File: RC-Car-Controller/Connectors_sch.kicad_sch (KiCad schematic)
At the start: 8 parts, among them J1 Conn_01x02, J5 MCU_IF, J6 ANT_IF, J7 2171790001, U2 USBLC6-2SC6

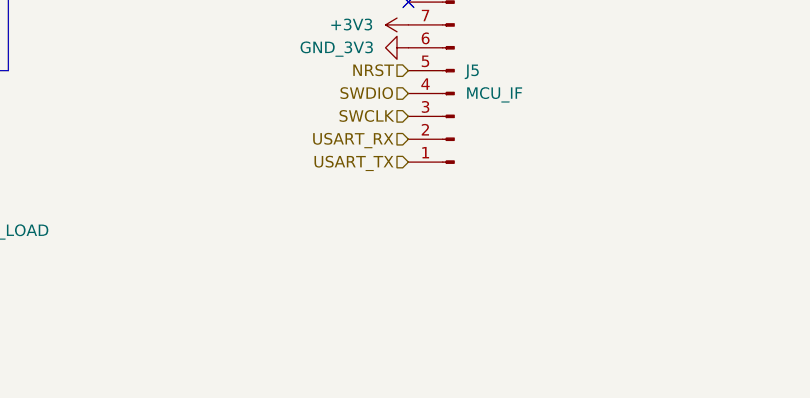
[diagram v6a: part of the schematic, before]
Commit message: Added FGH100M footprint/schematic
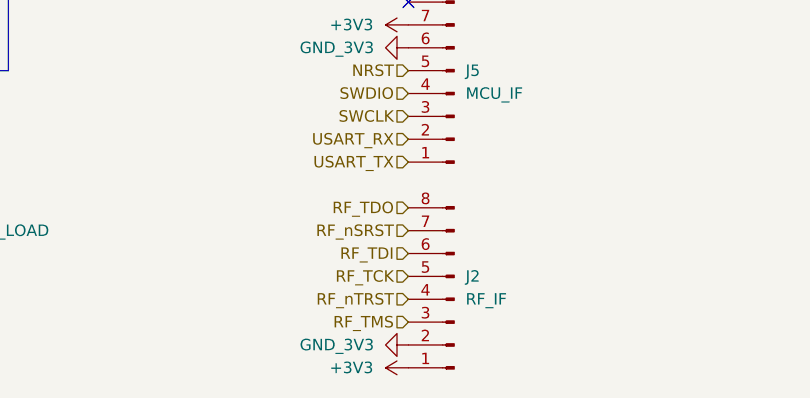
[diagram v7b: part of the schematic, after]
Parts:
- added J2: RF_IF, Connector_PinHeader_2.54mm:PinHeader_2x04_P2.54mm_Vertical, symbol Connector:Conn_01x08_Pin
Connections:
- net +3V3: now also J2.1 (Pin_1)
- net GND_3V3: now also J2.2 (Pin_2)
- new net RF_TCK: J2.5 (Pin_5)
- new net RF_TDI: J2.6 (Pin_6)
- new net RF_TDO: J2.8 (Pin_8)
- new net RF_TMS: J2.3 (Pin_3)
- new net RF_nSRST: J2.7 (Pin_7)
- new net RF_nTRST: J2.4 (Pin_4)

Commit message: Finished Controller PCB Pre-Review
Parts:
- renumbered J7 to J2, J5 to J3, J2 to J4, J6 to J5, R24 to R4, R23 to R5, U2 to U1
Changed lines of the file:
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@@
 		(on_board yes)
 		(dnp no)
-		(property "Reference" "U2"
+		(property "Reference" "U1"
 			(at 123.444 72.136 0)
 			(effects
@@
 			(project "RC-Car-Controller"
 				(path "/ba870fd1-751d-4755-8e1a-1ea86ca9e2f6/47812da9-b622-4bda-8507-4e09448e1ff5"
-					(reference "U2")
+					(reference "U1")
 					(unit 1)
 				)
@@
 		(dnp no)
 		(fields_autoplaced yes)
-		(property "Reference" "#PWR09"
+		(property "Reference" "#PWR031"
 			(at 127 129.54 0)
 			(effects
@@
 			(project "RC-Car-Project"
 				(path "/ba870fd1-751d-4755-8e1a-1ea86ca9e2f6/47812da9-b622-4bda-8507-4e09448e1ff5"
-					(reference "#PWR09")
+					(reference "#PWR031")
 					(unit 1)
 				)
@@
 		(dnp no)
 		(fields_autoplaced yes)
-		(property "Reference" "J5"
+		(property "Reference" "J3"
 			(at 129.54 134.6199 0)
 			(effects
@@
 			(project ""
 				(path "/ba870fd1-751d-4755-8e1a-1ea86ca9e2f6/47812da9-b622-4bda-8507-4e09448e1ff5"
-					(reference "J5")
+					(reference "J3")
 					(unit 1)
 				)
@@
 		(on_board yes)
 		(dnp no)
-		(property "Reference" "#PWR088"
+		(property "Reference" "#PWR028"
 			(at 104.14 110.49 0)
 			(effects
@@
 			(project "RC-Car-Controller"
 				(path "/ba870fd1-751d-4755-8e1a-1ea86ca9e2f6/47812da9-b622-4bda-8507-4e09448e1ff5"
-					(reference "#PWR088")
+					(reference "#PWR028")
 					(unit 1)
 				)
@@
 		(on_board yes)
 		(dnp no)
-		(property "Reference" "R24"
+		(property "Reference" "R4"
 			(at 104.14 90.678 90)
 			(effects
@@
 			(project "RC-Car-Controller"
 				(path "/ba870fd1-751d-4755-8e1a-1ea86ca9e2f6/47812da9-b622-4bda-8507-4e09448e1ff5"
-					(reference "R24")
+					(reference "R4")
 					(unit 1)
 				)
@@
 		(dnp no)
 		(fields_autoplaced yes)
-		(property "Reference" "J7"
+		(property "Reference" "J2"
 			(at 83.82 60.96 0)
 			(effects
@@
 			(project ""
 				(path "/ba870fd1-751d-4755-8e1a-1ea86ca9e2f6/47812da9-b622-4bda-8507-4e09448e1ff5"
-					(reference "J7")
+					(reference "J2")
 					(unit 1)
 				)
@@
 		(dnp no)
 		(fields_autoplaced yes)
-		(property "Reference" "#PWR013"
+		(property "Reference" "#PWR027"
 			(at 66.04 152.4 0)
 			(effects
@@
 			(project "RC-Car-Controller"
 				(path "/ba870fd1-751d-4755-8e1a-1ea86ca9e2f6/47812da9-b622-4bda-8507-4e09448e1ff5"
-					(reference "#PWR013")
+					(reference "#PWR027")
 					(unit 1)
 				)
@@
 		(dnp no)
 		(fields_autoplaced yes)
-		(property "Reference" "#PWR08"
+		(property "Reference" "#PWR032"
 			(at 116.84 132.08 0)
 			(effects
@@
 			(project "RC-Car-Project"
 				(path "/ba870fd1-751d-4755-8e1a-1ea86ca9e2f6/47812da9-b622-4bda-8507-4e09448e1ff5"
-					(reference "#PWR08")
+					(reference "#PWR032")
 					(unit 1)
 				)
@@
 		(dnp no)
 		(fields_autoplaced yes)
-		(property "Reference" "J2"
+		(property "Reference" "J4"
 			(at 129.54 157.4799 0)
 			(effects
@@
 			(project "RC-Car-Controller"
 				(path "/ba870fd1-751d-4755-8e1a-1ea86ca9e2f6/47812da9-b622-4bda-8507-4e09448e1ff5"
-					(reference "J2")
+					(reference "J4")
 					(unit 1)
 				)
@@
 		(dnp no)
 		(fields_autoplaced yes)
-		(property "Reference" "#PWR065"
+		(property "Reference" "#PWR033"
 			(at 116.84 165.1 0)
 			(effects
@@
 			(project "RC-Car-Controller"
 				(path "/ba870fd1-751d-4755-8e1a-1ea86ca9e2f6/47812da9-b622-4bda-8507-4e09448e1ff5"
-					(reference "#PWR065")
+					(reference "#PWR033")
 					(unit 1)
 				)
@@
 		(on_board yes)
 		(dnp no)
-		(property "Reference" "#PWR043"
+		(property "Reference" "#PWR030"
 			(at 121.92 95.25 0)
 			(effects
@@
 			(project "RC-Car-Controller"
 				(path "/ba870fd1-751d-4755-8e1a-1ea86ca9e2f6/47812da9-b622-4bda-8507-4e09448e1ff5"
-					(reference "#PWR043")
+					(reference "#PWR030")
 					(unit 1)
 				)
@@
 		(on_board yes)
 		(dnp no)
-		(property "Reference" "#PWR087"
+		(property "Reference" "#PWR026"
 			(at 50.8 81.28 0)
 			(effects
@@
 			(project "RC-Car-Controller"
 				(path "/ba870fd1-751d-4755-8e1a-1ea86ca9e2f6/47812da9-b622-4bda-8507-4e09448e1ff5"
-					(reference "#PWR087")
+					(reference "#PWR026")
 					(unit 1)
 				)
@@
 		(on_board yes)
 		(dnp no)
-		(property "Reference" "#PWR042"
+		(property "Reference" "#PWR029"
 			(at 121.92 64.77 0)
 			(effects
@@
 			(project "RC-Car-Controller"
 				(path "/ba870fd1-751d-4755-8e1a-1ea86ca9e2f6/47812da9-b622-4bda-8507-4e09448e1ff5"
-					(reference "#PWR042")
+					(reference "#PWR029")
 					(unit 1)
 				)
@@
 		(dnp no)
 		(fields_autoplaced yes)
-		(property "Reference" "#PWR096"
+		(property "Reference" "#PWR022"
 			(at 58.42 152.4 0)
 			(effects
@@
 			(project "RC-Car-Controller"
 				(path "/ba870fd1-751d-4755-8e1a-1ea86ca9e2f6/47812da9-b622-4bda-8507-4e09448e1ff5"
-					(reference "#PWR096")
+					(reference "#PWR022")
 					(unit 1)
 				)
@@
 		(dnp no)
 		(fields_autoplaced yes)
-		(property "Reference" "#PWR092"
+		(property "Reference" "#PWR023"
 			(at 59.69 129.54 0)
 			(effects
@@
 			(project "RC-Car-Project"
 				(path "/ba870fd1-751d-4755-8e1a-1ea86ca9e2f6/47812da9-b622-4bda-8507-4e09448e1ff5"
-					(reference "#PWR092")
+					(reference "#PWR023")
 					(unit 1)
 				)
@@
 		(on_board yes)
 		(dnp no)
-		(property "Reference" "R23"
+		(property "Reference" "R5"
 			(at 106.68 90.678 90)
 			(effects
@@
 			(project "RC-Car-Controller"
 				(path "/ba870fd1-751d-4755-8e1a-1ea86ca9e2f6/47812da9-b622-4bda-8507-4e09448e1ff5"
-					(reference "R23")
+					(reference "R5")
 					(unit 1)
 				)
@@
 		(dnp no)
 		(fields_autoplaced yes)
-		(property "Reference" "#PWR064"
+		(property "Reference" "#PWR034"
 			(at 127 167.64 0)
 			(effects
@@
 			(project "RC-Car-Controller"
 				(path "/ba870fd1-751d-4755-8e1a-1ea86ca9e2f6/47812da9-b622-4bda-8507-4e09448e1ff5"
-					(reference "#PWR064")
+					(reference "#PWR034")
 					(unit 1)
 				)
@@
 		(dnp no)
 		(fields_autoplaced yes)
-		(property "Reference" "#PWR093"
+		(property "Reference" "#PWR024"
 			(at 49.53 132.08 0)
 			(effects
@@
 			(project "RC-Car-Project"
 				(path "/ba870fd1-751d-4755-8e1a-1ea86ca9e2f6/47812da9-b622-4bda-8507-4e09448e1ff5"
-					(reference "#PWR093")
+					(reference "#PWR024")
 					(unit 1)
 				)
@@
 		(dnp no)
 		(fields_autoplaced yes)
-		(property "Reference" "#PWR091"
+		(property "Reference" "#PWR035"
 			(at 187.96 135.89 0)
 			(effects
@@
 			(project "RC-Car-Project"
 				(path "/ba870fd1-751d-4755-8e1a-1ea86ca9e2f6/47812da9-b622-4bda-8507-4e09448e1ff5"
-					(reference "#PWR091")
+					(reference "#PWR035")
 					(unit 1)
 				)
@@
 		(on_board yes)
 		(dnp no)
-		(property "Reference" "#PWR086"
+		(property "Reference" "#PWR025"
 			(at 50.8 76.2 0)
 			(effects
@@
 			(project "RC-Car-Controller"
 				(path "/ba870fd1-751d-4755-8e1a-1ea86ca9e2f6/47812da9-b622-4bda-8507-4e09448e1ff5"
-					(reference "#PWR086")
+					(reference "#PWR025")
 					(unit 1)
 				)
@@
 		(dnp no)
 		(fields_autoplaced yes)
-		(property "Reference" "J6"
+		(property "Reference" "J5"
 			(at 178.5504 129.54 0)
 			(effects
@@
 			(project ""
 				(path "/ba870fd1-751d-4755-8e1a-1ea86ca9e2f6/47812da9-b622-4bda-8507-4e09448e1ff5"
-					(reference "J6")
-					(unit 1)
-				)
+					(reference "J5")
+					(unit 1)
+				)
